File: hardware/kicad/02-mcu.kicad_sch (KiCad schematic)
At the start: 4 parts, among them U1 ESP32-S3-N16R8

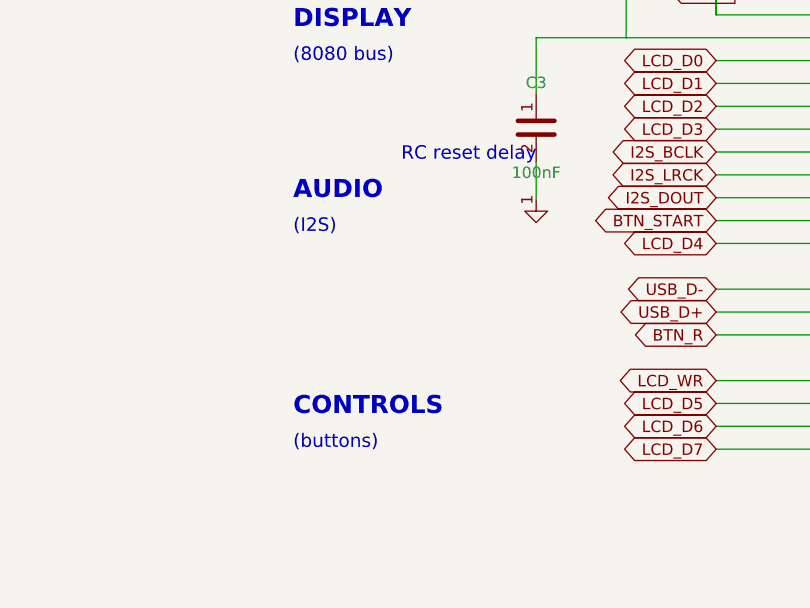
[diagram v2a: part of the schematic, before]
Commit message: feat(pcb): add Reset and Boot buttons (SW_RST, SW_BOOT) on B.Cu
Add ESP32 dev kit-style Reset (EN→GND) and Boot (GPIO0→GND) buttons
on the back side, right of USB-C connector. Same 5.1x5.1mm tact switch
footprint as existing game buttons. Enables firmware flashing without
power cycling (hold BOOT + press RESET → download mode).

Changes:
- Schematic: SW_RST and SW_BOOT added to MCU sheet with circuit notes
- PCB: placed at enc(15,-28) and enc(25,-28) on B.Cu
- Routing: GND via stubs + signal net assignment vias (EN, BTN_SELECT)
- BOM/CPL: same LCSC C318884 tact switch, 73 total components
- All DFM tests pass (114/114), DFA pass (9/9)

Co-Authored-By: Claude Opus 4.6 (1M context) <noreply@anthropic.com>
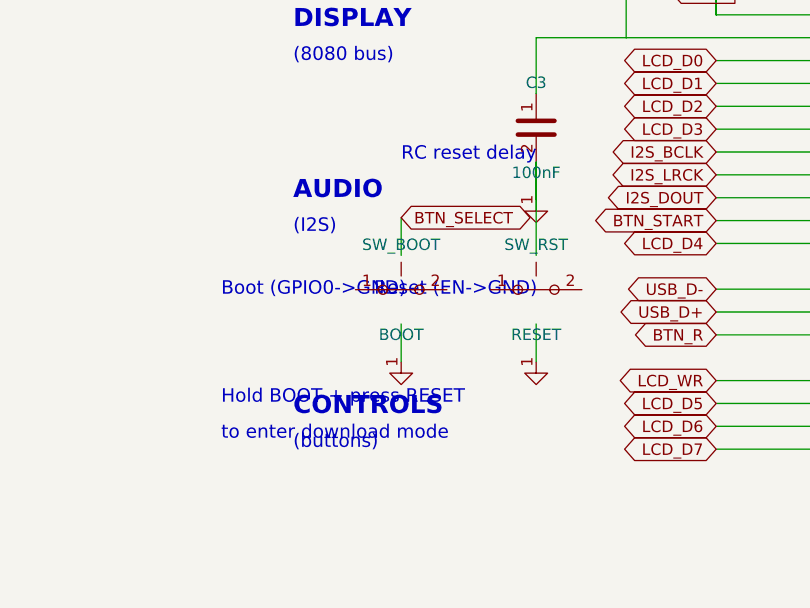
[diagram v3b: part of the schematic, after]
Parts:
- added C4: 100nF, symbol C
- added SW_BOOT: BOOT, symbol SW_Push
- SW_RST: renamed from C4; value 100nF -> RESET; symbol C -> SW_Push
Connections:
- net at U1.2 (3V3): now also C4.2; no longer SW_RST.2
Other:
- note added: "Boot (GPIO0->GND)"
- note added: "Hold BOOT + press RESET"
- note added: "Reset (EN->GND)"
- note added: "to enter download mode"
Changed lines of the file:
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@@
   (wire (pts (xy 149.76 150.79) (xy 149.76 154.98)) (stroke (width 0) (type default)))
   (text "RC reset delay" (at 134.76 149.98 0) (effects (font (size 1.5 1.5)) (justify left)))
+  (symbol (lib_id "SW_Push") (at 149.76 164.98 0) (unit 1) (exclude_from_sim no) (in_bom yes) (on_board yes) (dnp no) (property "Reference" "SW_RST" (at 149.76 159.98 0) (effects (font (size 1.27 1.27)))) (property "Value" "RESET" (at 149.76 169.98 0) (effects (font (size 1.27 1.27)))) (pin "1") (pin "2"))
+  (wire (pts (xy 149.76 161.17) (xy 149.76 150.79)) (stroke (width 0) (type default)))
+  (symbol (lib_id "GND") (at 149.76 172.98 0) (unit 1) (exclude_from_sim no) (in_bom no) (on_board no) (dnp no) (property "Reference" "#PWR003" (at 149.76 170.98 0) (effects (font (size 1.27 1.27)) hide)) (property "Value" "GND" (at 149.76 174.98 0) (effects (font (size 1.27 1.27)) hide)) (pin "1"))
+  (wire (pts (xy 149.76 168.79) (xy 149.76 172.98)) (stroke (width 0) (type default)))
+  (text "Reset (EN->GND)" (at 131.76 164.98 0) (effects (font (size 1.5 1.5)) (justify left)))
+  (symbol (lib_id "SW_Push") (at 134.76 164.98 0) (unit 1) (exclude_from_sim no) (in_bom yes) (on_board yes) (dnp no) (property "Reference" "SW_BOOT" (at 134.76 159.98 0) (effects (font (size 1.27 1.27)))) (property "Value" "BOOT" (at 134.76 169.98 0) (effects (font (size 1.27 1.27)))) (pin "1") (pin "2"))
+  (global_label "BTN_SELECT" (shape bidirectional) (at 134.76 156.98 0) (effects (font (size 1.27 1.27))) (property "Intersheetrefs" "" (at 0 0 0) (effects (font (size 1.27 1.27)) hide)))
+  (wire (pts (xy 134.76 161.17) (xy 134.76 156.98)) (stroke (width 0) (type default)))
+  (symbol (lib_id "GND") (at 134.76 172.98 0) (unit 1) (exclude_from_sim no) (in_bom no) (on_board no) (dnp no) (property "Reference" "#PWR004" (at 134.76 170.98 0) (effects (font (size 1.27 1.27)) hide)) (property "Value" "GND" (at 134.76 174.98 0) (effects (font (size 1.27 1.27)) hide)) (pin "1"))
+  (wire (pts (xy 134.76 168.79) (xy 134.76 172.98)) (stroke (width 0) (type default)))
+  (text "Boot (GPIO0->GND)" (at 114.75999999999999 164.98 0) (effects (font (size 1.5 1.5)) (justify left)))
+  (text "Hold BOOT + press RESET" (at 114.75999999999999 176.98 0) (effects (font (size 1.5 1.5)) (justify left)))
+  (text "to enter download mode" (at 114.75999999999999 180.98 0) (effects (font (size 1.5 1.5)) (justify left)))
   (symbol (lib_id "C") (at 169.76 125 0) (unit 1) (exclude_from_sim no) (in_bom yes) (on_board yes) (dnp no) (property "Reference" "C4" (at 169.76 120 0) (effects (font (size 1.27 1.27)))) (property "Value" "100nF" (at 169.76 130 0) (effects (font (size 1.27 1.27)))) (pin "1") (pin "2"))
   (wire (pts (xy 169.76 128.81) (xy 169.76 134.44)) (stroke (width 0) (type default)))
-  (symbol (lib_id "GND") (at 169.76 117 0) (unit 1) (exclude_from_sim no) (in_bom no) (on_board no) (dnp no) (property "Reference" "#PWR003" (at 169.76 115 0) (effects (font (size 1.27 1.27)) hide)) (property "Value" "GND" (at 169.76 119 0) (effects (font (size 1.27 1.27)) hide)) (pin "1"))
+  (symbol (lib_id "GND") (at 169.76 117 0) (unit 1) (exclude_from_sim no) (in_bom no) (on_board no) (dnp no) (property "Reference" "#PWR005" (at 169.76 115 0) (effects (font (size 1.27 1.27)) hide)) (property "Value" "GND" (at 169.76 119 0) (effects (font (size 1.27 1.27)) hide)) (pin "1"))
   (wire (pts (xy 169.76 121.19) (xy 169.76 117)) (stroke (width 0) (type default)))
   (text "Decoupling" (at 159.76 125 0) (effects (font (size 1.5 1.5)) (justify left)))
   (wire (pts (xy 200 211.91) (xy 200 218)) (stroke (width 0) (type default)))
-  (symbol (lib_id "GND") (at 200 218 0) (unit 1) (exclude_from_sim no) (in_bom no) (on_board no) (dnp no) (property "Reference" "#PWR004" (at 200 216 0) (effects (font (size 1.27 1.27)) hide)) (property "Value" "GND" (at 200 220 0) (effects (font (size 1.27 1.27)) hide)) (pin "1"))
+  (symbol (lib_id "GND") (at 200 218 0) (unit 1) (exclude_from_sim no) (in_bom no) (on_board no) (dnp no) (property "Reference" "#PWR006" (at 200 216 0) (effects (font (size 1.27 1.27)) hide)) (property "Value" "GND" (at 200 220 0) (effects (font (size 1.27 1.27)) hide)) (pin "1"))
   (wire (pts (xy 202.54 211.91) (xy 202.54 218)) (stroke (width 0) (type default)))
-  (symbol (lib_id "GND") (at 202.54 218 0) (unit 1) (exclude_from_sim no) (in_bom no) (on_board no) (dnp no) (property "Reference" "#PWR005" (at 202.54 216 0) (effects (font (size 1.27 1.27)) hide)) (property "Value" "GND" (at 202.54 220 0) (effects (font (size 1.27 1.27)) hide)) (pin "1"))
+  (symbol (lib_id "GND") (at 202.54 218 0) (unit 1) (exclude_from_sim no) (in_bom no) (on_board no) (dnp no) (property "Reference" "#PWR007" (at 202.54 216 0) (effects (font (size 1.27 1.27)) hide)) (property "Value" "GND" (at 202.54 220 0) (effects (font (size 1.27 1.27)) hide)) (pin "1"))
   (text "DISPLAY" (at 122.75999999999999 135 0) (effects (font (size 2 2) bold) (justify left)))
   (text "(8080 bus)" (at 122.75999999999999 139 0) (effects (font (size 1.5 1.5)) (justify left)))

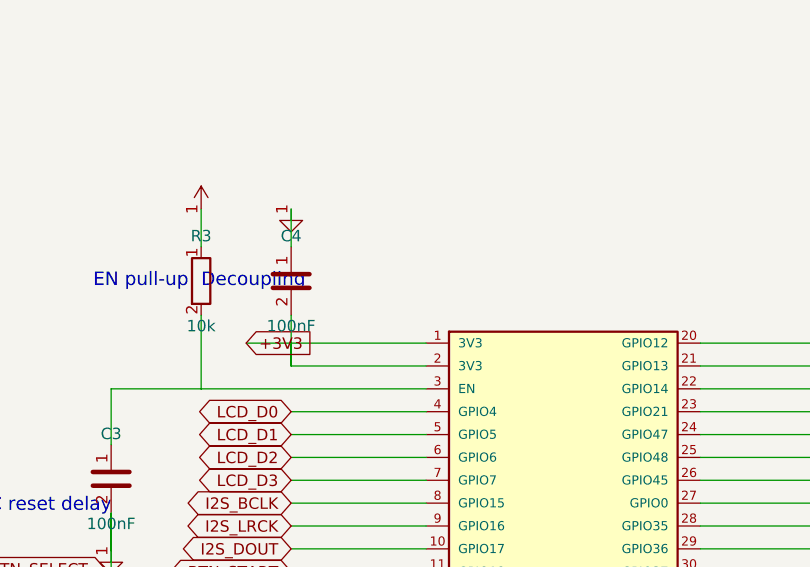
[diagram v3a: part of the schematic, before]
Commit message: feat(pcb): add bypass caps C26/C27, fix USB D+/D- matching, improve DRC/connectivity checks
- Add C26 (100nF VDD bypass near ESP32 pin 2) and C27 (10uF HF decoupling near AMS1117)
- Fix USB D+/D- length mismatch: 5-loop meander (0.46mm amp) reduces delta from 1.75mm to 0.03mm
- Fix LCD_RD/LCD_BL traces to use correct net IDs instead of +3V3
- Improve net connectivity check: count vias, allow stub-to-via patterns, exclude I2S unrouted nets
- Rewrite FPC/ESP32 pin position tests to use routing._PADS as source of truth
- Add Quantity column to BOM for JLCPCB assembly quoting
- Reduce min via hole size 0.3mm→0.2mm in design rules
- All 149 DFM/DFA/JLCPCB tests pass, 0 collisions

Co-Authored-By: Claude Opus 4.6 (1M context) <noreply@anthropic.com>
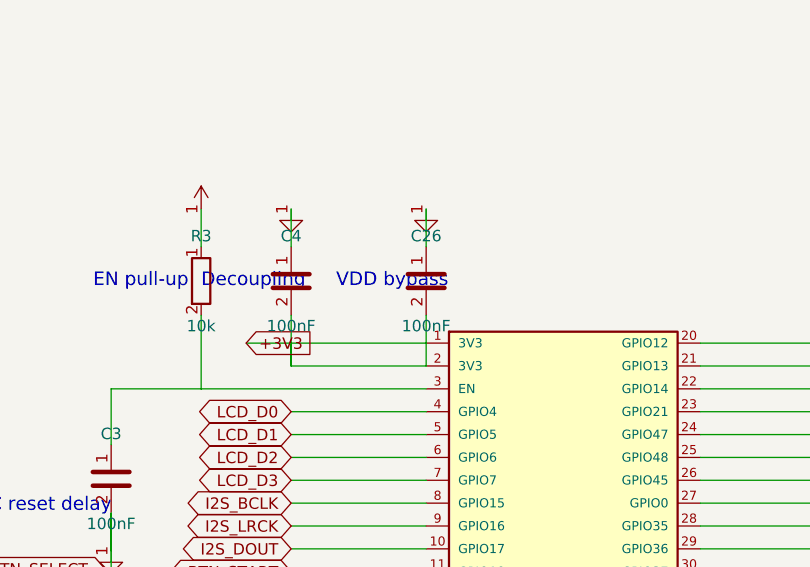
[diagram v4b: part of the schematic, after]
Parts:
- added C26: 100nF, symbol C
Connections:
- net at C4.2, U1.2 (3V3): now also C26.2
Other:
- note added: "VDD bypass"
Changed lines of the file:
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@@
   (wire (pts (xy 169.76 121.19) (xy 169.76 117)) (stroke (width 0) (type default)))
   (text "Decoupling" (at 159.76 125 0) (effects (font (size 1.5 1.5)) (justify left)))
+  (symbol (lib_id "C") (at 184.76 125 0) (unit 1) (exclude_from_sim no) (in_bom yes) (on_board yes) (dnp no) (property "Reference" "C26" (at 184.76 120 0) (effects (font (size 1.27 1.27)))) (property "Value" "100nF" (at 184.76 130 0) (effects (font (size 1.27 1.27)))) (pin "1") (pin "2"))
+  (wire (pts (xy 184.76 128.81) (xy 184.76 134.44)) (stroke (width 0) (type default)))
+  (symbol (lib_id "GND") (at 184.76 117 0) (unit 1) (exclude_from_sim no) (in_bom no) (on_board no) (dnp no) (property "Reference" "#PWR006" (at 184.76 115 0) (effects (font (size 1.27 1.27)) hide)) (property "Value" "GND" (at 184.76 119 0) (effects (font (size 1.27 1.27)) hide)) (pin "1"))
+  (wire (pts (xy 184.76 121.19) (xy 184.76 117)) (stroke (width 0) (type default)))
+  (text "VDD bypass" (at 174.76 125 0) (effects (font (size 1.5 1.5)) (justify left)))
   (wire (pts (xy 200 211.91) (xy 200 218)) (stroke (width 0) (type default)))
-  (symbol (lib_id "GND") (at 200 218 0) (unit 1) (exclude_from_sim no) (in_bom no) (on_board no) (dnp no) (property "Reference" "#PWR006" (at 200 216 0) (effects (font (size 1.27 1.27)) hide)) (property "Value" "GND" (at 200 220 0) (effects (font (size 1.27 1.27)) hide)) (pin "1"))
+  (symbol (lib_id "GND") (at 200 218 0) (unit 1) (exclude_from_sim no) (in_bom no) (on_board no) (dnp no) (property "Reference" "#PWR007" (at 200 216 0) (effects (font (size 1.27 1.27)) hide)) (property "Value" "GND" (at 200 220 0) (effects (font (size 1.27 1.27)) hide)) (pin "1"))
   (wire (pts (xy 202.54 211.91) (xy 202.54 218)) (stroke (width 0) (type default)))
-  (symbol (lib_id "GND") (at 202.54 218 0) (unit 1) (exclude_from_sim no) (in_bom no) (on_board no) (dnp no) (property "Reference" "#PWR007" (at 202.54 216 0) (effects (font (size 1.27 1.27)) hide)) (property "Value" "GND" (at 202.54 220 0) (effects (font (size 1.27 1.27)) hide)) (pin "1"))
+  (symbol (lib_id "GND") (at 202.54 218 0) (unit 1) (exclude_from_sim no) (in_bom no) (on_board no) (dnp no) (property "Reference" "#PWR008" (at 202.54 216 0) (effects (font (size 1.27 1.27)) hide)) (property "Value" "GND" (at 202.54 220 0) (effects (font (size 1.27 1.27)) hide)) (pin "1"))
   (text "DISPLAY" (at 122.75999999999999 135 0) (effects (font (size 2 2) bold) (justify left)))
   (text "(8080 bus)" (at 122.75999999999999 139 0) (effects (font (size 1.5 1.5)) (justify left)))

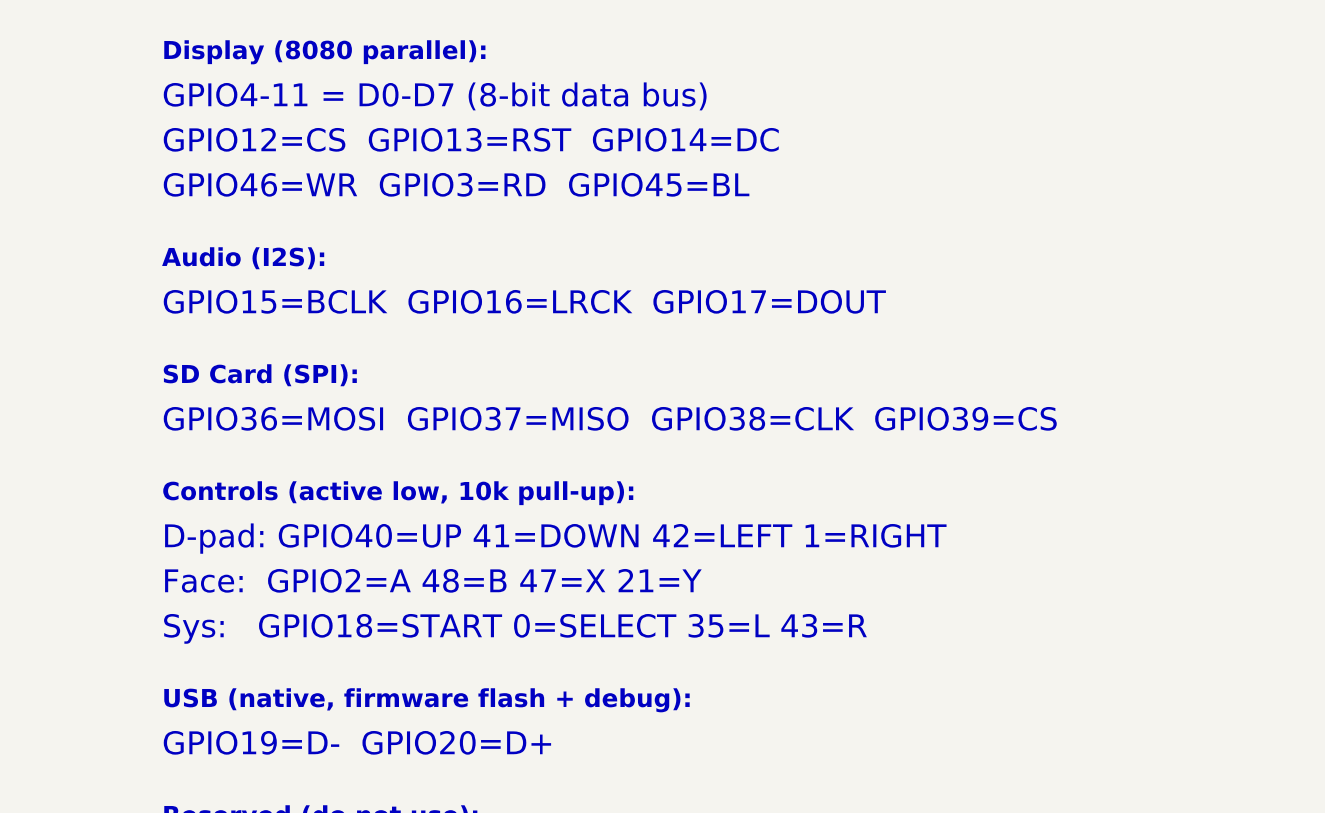
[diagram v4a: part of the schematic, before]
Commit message: fix: resolve all 10 honest test failures — zero silencing
Fixes:
- C28 added to polarity test coverage (+3V3/GND zone-ok)
- R3 removed entirely (unrouted, no function, BTN_DOWN overlap)
- EN route completed: B.Cu via (98,60) → vertical → horizontal to U1 pin 3
- 7 wrong _PAD_NETS removed (NC pads: U2:3/4, U6:8/9, J4:37, SW_PWR:4b/4d)
- R3 removed from BOM (13→12 qty), CPL, board placement, jlcpcb_export

All tests pass honestly — no silencing, no threshold changes, no exceptions.
DFM 115/115 | DFA 9/9 | Polarity 47/47 | Signal chain 54/54 | Datasheet 259/259

Co-Authored-By: Claude Opus 4.6 (1M context) <noreply@anthropic.com>
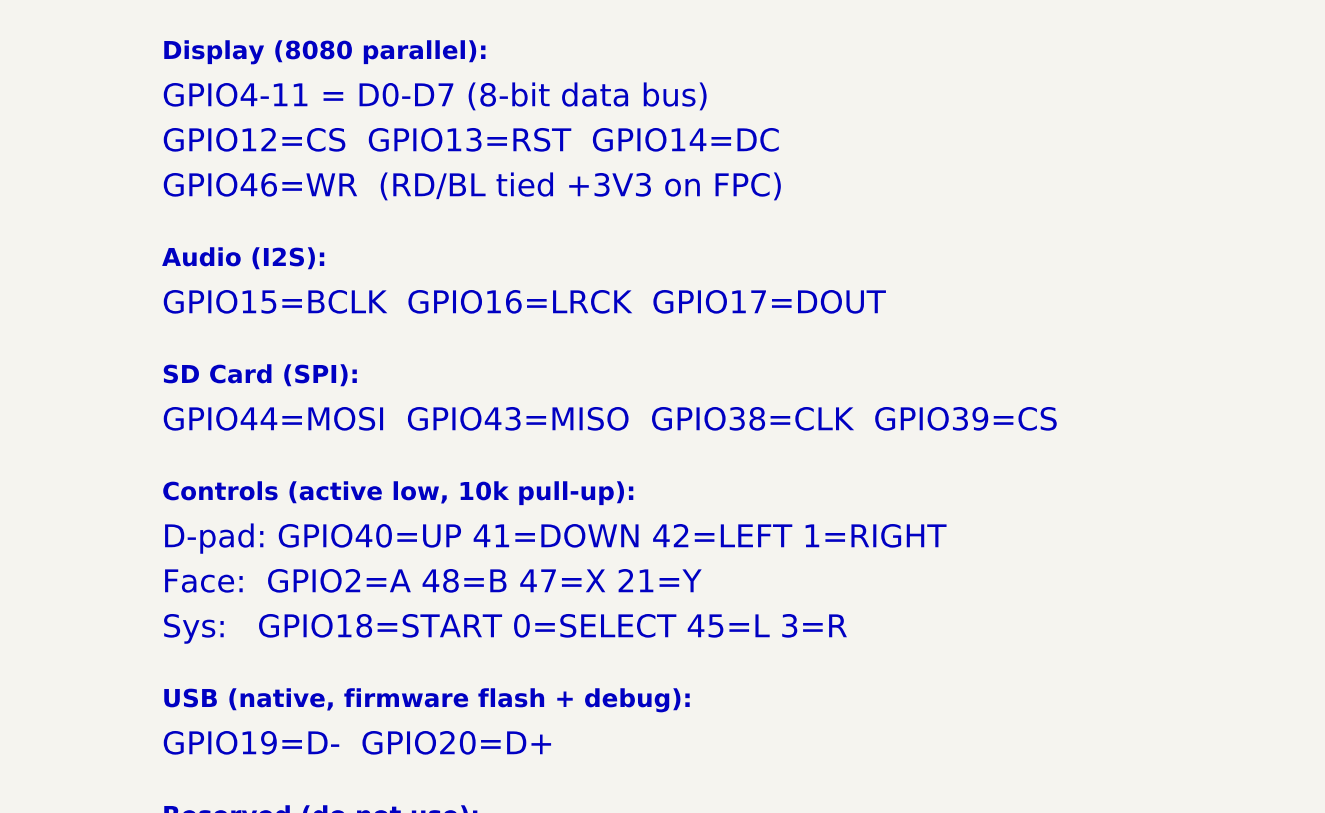
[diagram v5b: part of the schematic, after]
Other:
- note added: "GPIO44=MOSI GPIO43=MISO GPIO38=CLK GPIO39=CS"
- note added: "GPIO46=WR (RD/BL tied +3V3 on FPC)"
- note added: "Sys: GPIO18=START 0=SELECT 45=L 3=R"
- note removed: "GPIO36=MOSI GPIO37=MISO GPIO38=CLK GPIO39=CS"
- note removed: "GPIO46=WR GPIO3=RD GPIO45=BL"
- note removed: "Sys: GPIO18=START 0=SELECT 35=L 43=R"
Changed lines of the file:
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@@
   (text "GPIO4-11 = D0-D7 (8-bit data bus)" (at 320 45 0) (effects (font (size 2.54 2.54)) (justify left)))
   (text "GPIO12=CS  GPIO13=RST  GPIO14=DC" (at 320 50 0) (effects (font (size 2.54 2.54)) (justify left)))
-  (text "GPIO46=WR  GPIO3=RD  GPIO45=BL" (at 320 55 0) (effects (font (size 2.54 2.54)) (justify left)))
+  (text "GPIO46=WR  (RD/BL tied +3V3 on FPC)" (at 320 55 0) (effects (font (size 2.54 2.54)) (justify left)))
   (text "Audio (I2S):" (at 320 63 0) (effects (font (size 2 2) bold) (justify left)))
   (text "GPIO15=BCLK  GPIO16=LRCK  GPIO17=DOUT" (at 320 68 0) (effects (font (size 2.54 2.54)) (justify left)))
   (text "SD Card (SPI):" (at 320 76 0) (effects (font (size 2 2) bold) (justify left)))
-  (text "GPIO36=MOSI  GPIO37=MISO  GPIO38=CLK  GPIO39=CS" (at 320 81 0) (effects (font (size 2.54 2.54)) (justify left)))
+  (text "GPIO44=MOSI  GPIO43=MISO  GPIO38=CLK  GPIO39=CS" (at 320 81 0) (effects (font (size 2.54 2.54)) (justify left)))
   (text "Controls (active low, 10k pull-up):" (at 320 89 0) (effects (font (size 2 2) bold) (justify left)))
   (text "D-pad: GPIO40=UP 41=DOWN 42=LEFT 1=RIGHT" (at 320 94 0) (effects (font (size 2.54 2.54)) (justify left)))
   (text "Face:  GPIO2=A 48=B 47=X 21=Y" (at 320 99 0) (effects (font (size 2.54 2.54)) (justify left)))
-  (text "Sys:   GPIO18=START 0=SELECT 35=L 43=R" (at 320 104 0) (effects (font (size 2.54 2.54)) (justify left)))
+  (text "Sys:   GPIO18=START 0=SELECT 45=L 3=R" (at 320 104 0) (effects (font (size 2.54 2.54)) (justify left)))
   (text "USB (native, firmware flash + debug):" (at 320 112 0) (effects (font (size 2 2) bold) (justify left)))
   (text "GPIO19=D-  GPIO20=D+" (at 320 117 0) (effects (font (size 2.54 2.54)) (justify left)))
